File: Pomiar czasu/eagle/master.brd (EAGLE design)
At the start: 119 x 107.9 mm, 51 parts, among them IC1 MEGA8-AI, IC2 lf33, U2 RFM69HW

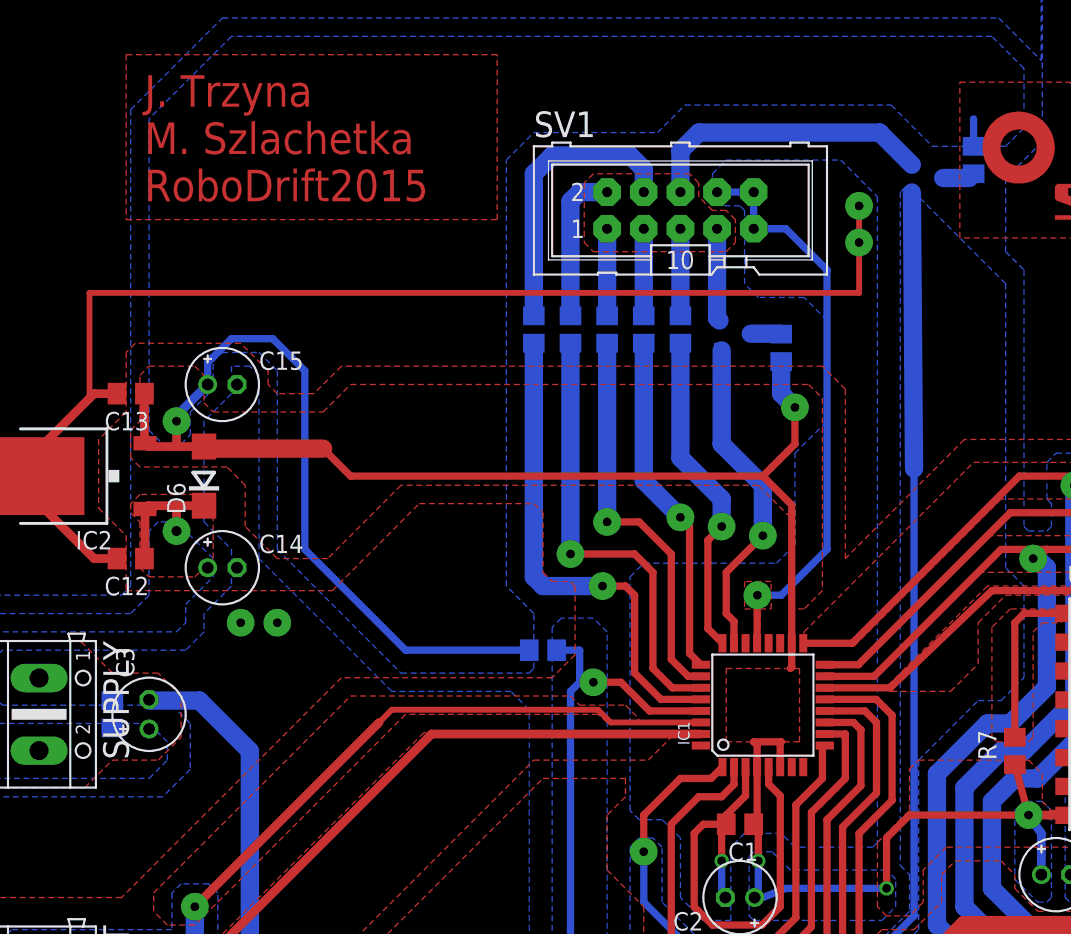
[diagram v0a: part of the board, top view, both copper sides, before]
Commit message: Slave->ctc, tsal modulation
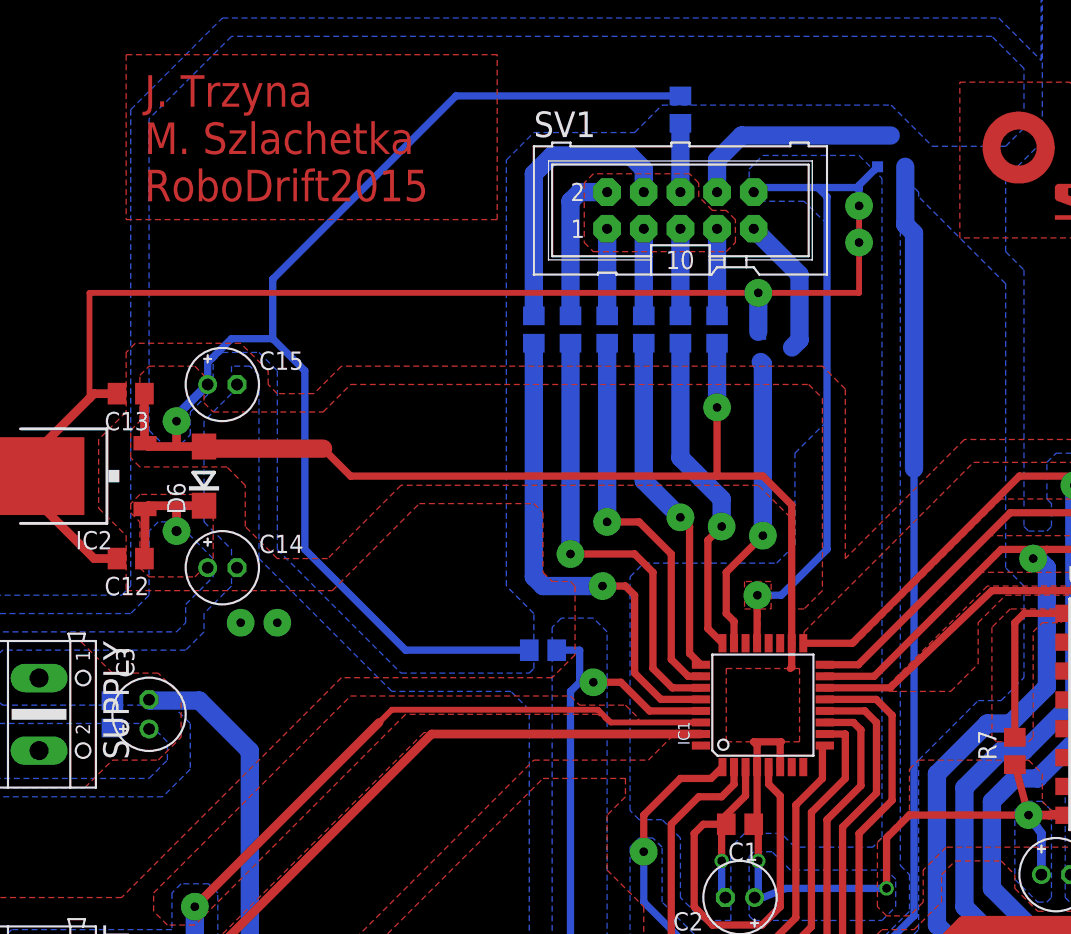
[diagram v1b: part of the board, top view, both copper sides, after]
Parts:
- moved R30 20.6 mm to (57.8, 92.7)
- moved R2 4.62 mm to (60.3, 77.5)
- moved Q4 3.18 mm to (72.4, 89.9), turned to 0 degrees
- moved Q3 3.01 mm to (64.5, 76.2)
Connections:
- removed net N$1: Q3.3, R2.1
- removed net N$2: Q4.3, R30.1
- new net LED_FALSTART_GND: Q4.3, SV1.8
- new net LED_GO_GND: Q3.3, SV1.9
- net GND: now also Q3.2, Q4.2; no longer SV1.8, SV1.9
- net LED_FALSTART: now also R30.1; no longer Q4.2
- net LED_GO: now also R2.1; no longer Q3.2
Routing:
- net +3V3: track 173.9 -> 209.5 mm
- net LED_FALSTART: track 20.4 -> 4.77 mm
- net LED_FALSTART_GND: track 0.00 -> 15.0 mm
- net LED_GO_GND: track 0.00 -> 9.76 mm
- net GND: track 436.8 -> 445.1 mm, vias 8 -> 9
- net N$2: track 2.23 -> 0.00 mm
- net LED_GO_GATE: track 23.0 -> 20.8 mm
- net N$1: track 2.12 -> 0.00 mm
- net LED_FALSTART_GATE: track 83.4 -> 85.5 mm

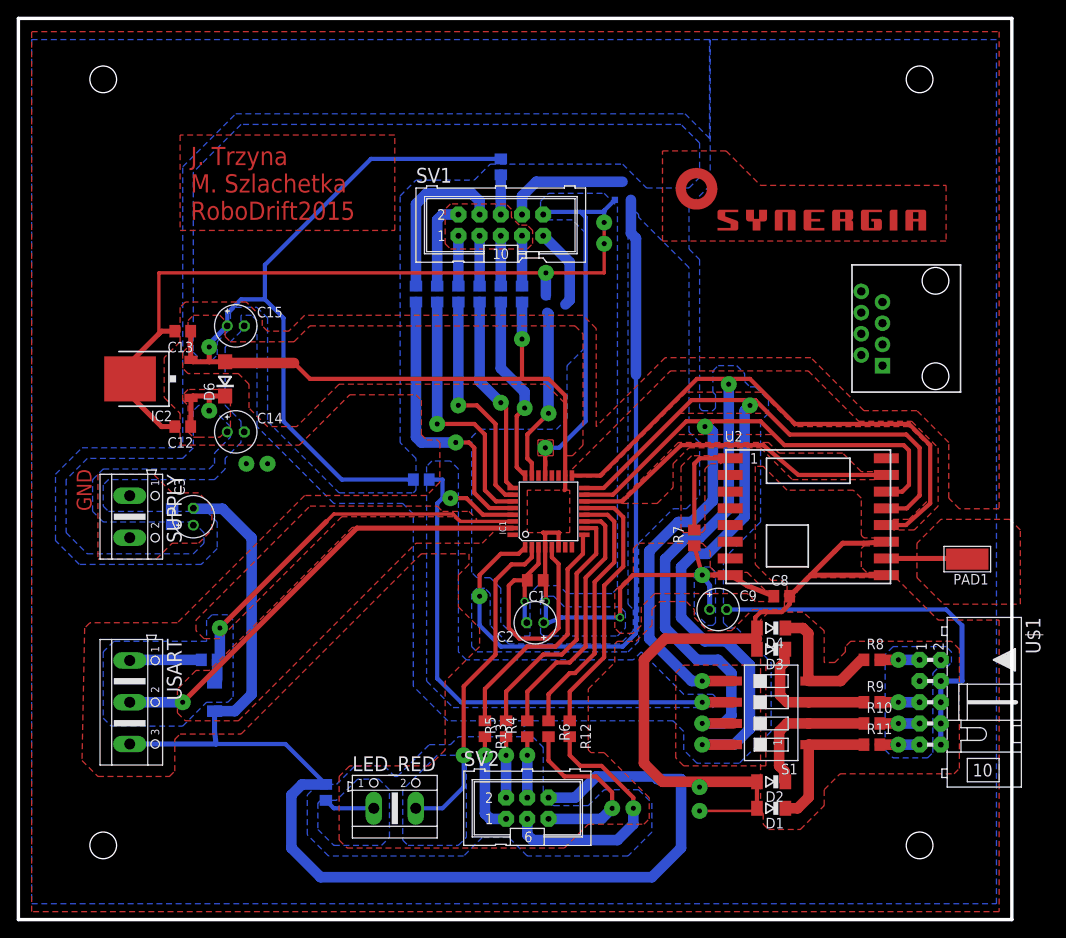
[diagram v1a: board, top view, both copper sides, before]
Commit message: RFM69:communication master->sensor works!
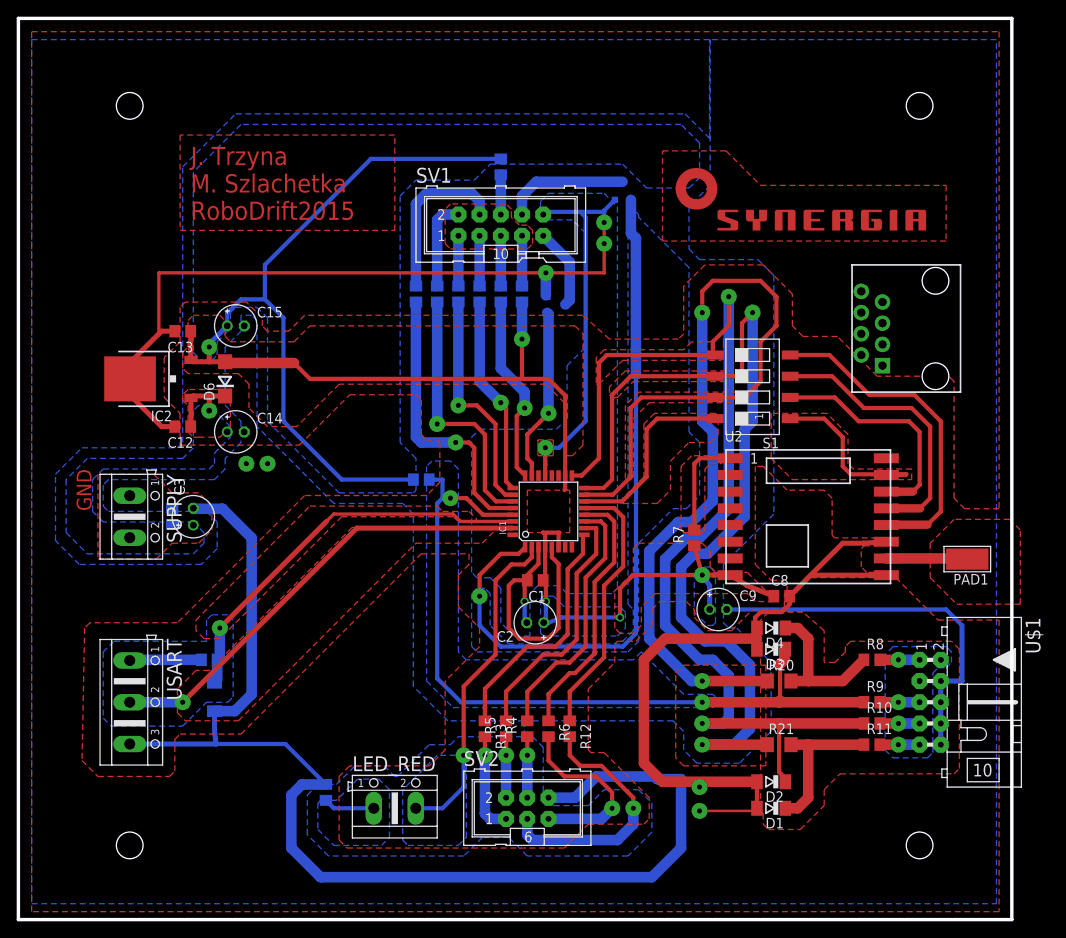
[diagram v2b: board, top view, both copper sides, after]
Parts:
- added R20, R21: 0R, rcl:R1206
- moved S1 39.1 mm to (87.9, 66.4)
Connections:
- new net DIO0: IC1.32, U2.2
- new net N$1: D1.C, R11.1, R21.2
- new net N$2: D4.C, R20.2, R8.1
- net MISO: now also R21.1, S1.6; no longer S1.8, U2.13
- net MOSI: now also R20.1, S1.7; no longer S1.5, U2.14
- net N$10: now also S1.4, U2.12; no longer D3.C, R9.1, S1.3
- net N$11: now also S1.3, U2.13; no longer D2.C, R10.1, S1.2
- net N$12: now also S1.2, U2.14; no longer D1.C, R11.1, S1.1
- net N$8: now also S1.1, U2.15; no longer D4.C, R8.1, S1.4
- net RESET: now also D3.C, R9.1; no longer S1.6
- net SCK: now also D2.C, R10.1, S1.5; no longer S1.7, U2.12
- net SS: now also S1.8; no longer U2.15
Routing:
- net N$10: track 16.2 -> 39.3 mm
- net RESET: track 71.6 -> 93.9 mm
- net MOSI: track 94.6 -> 115.2 mm
- net N$1: track 0.00 -> 18.4 mm
- net N$2: track 0.00 -> 18.1 mm
- net SS: track 40.2 -> 23.1 mm
- net N$11: track 17.4 -> 33.6 mm
- net N$12: track 16.3 -> 27.9 mm
- net SCK: track 121.1 -> 126.4 mm
- net N$8: track 16.4 -> 21.2 mm
- net MISO: track 116.4 -> 111.7 mm
- added copper zone on layer 1, net N$8
